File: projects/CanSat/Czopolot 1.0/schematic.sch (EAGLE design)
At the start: 16 parts

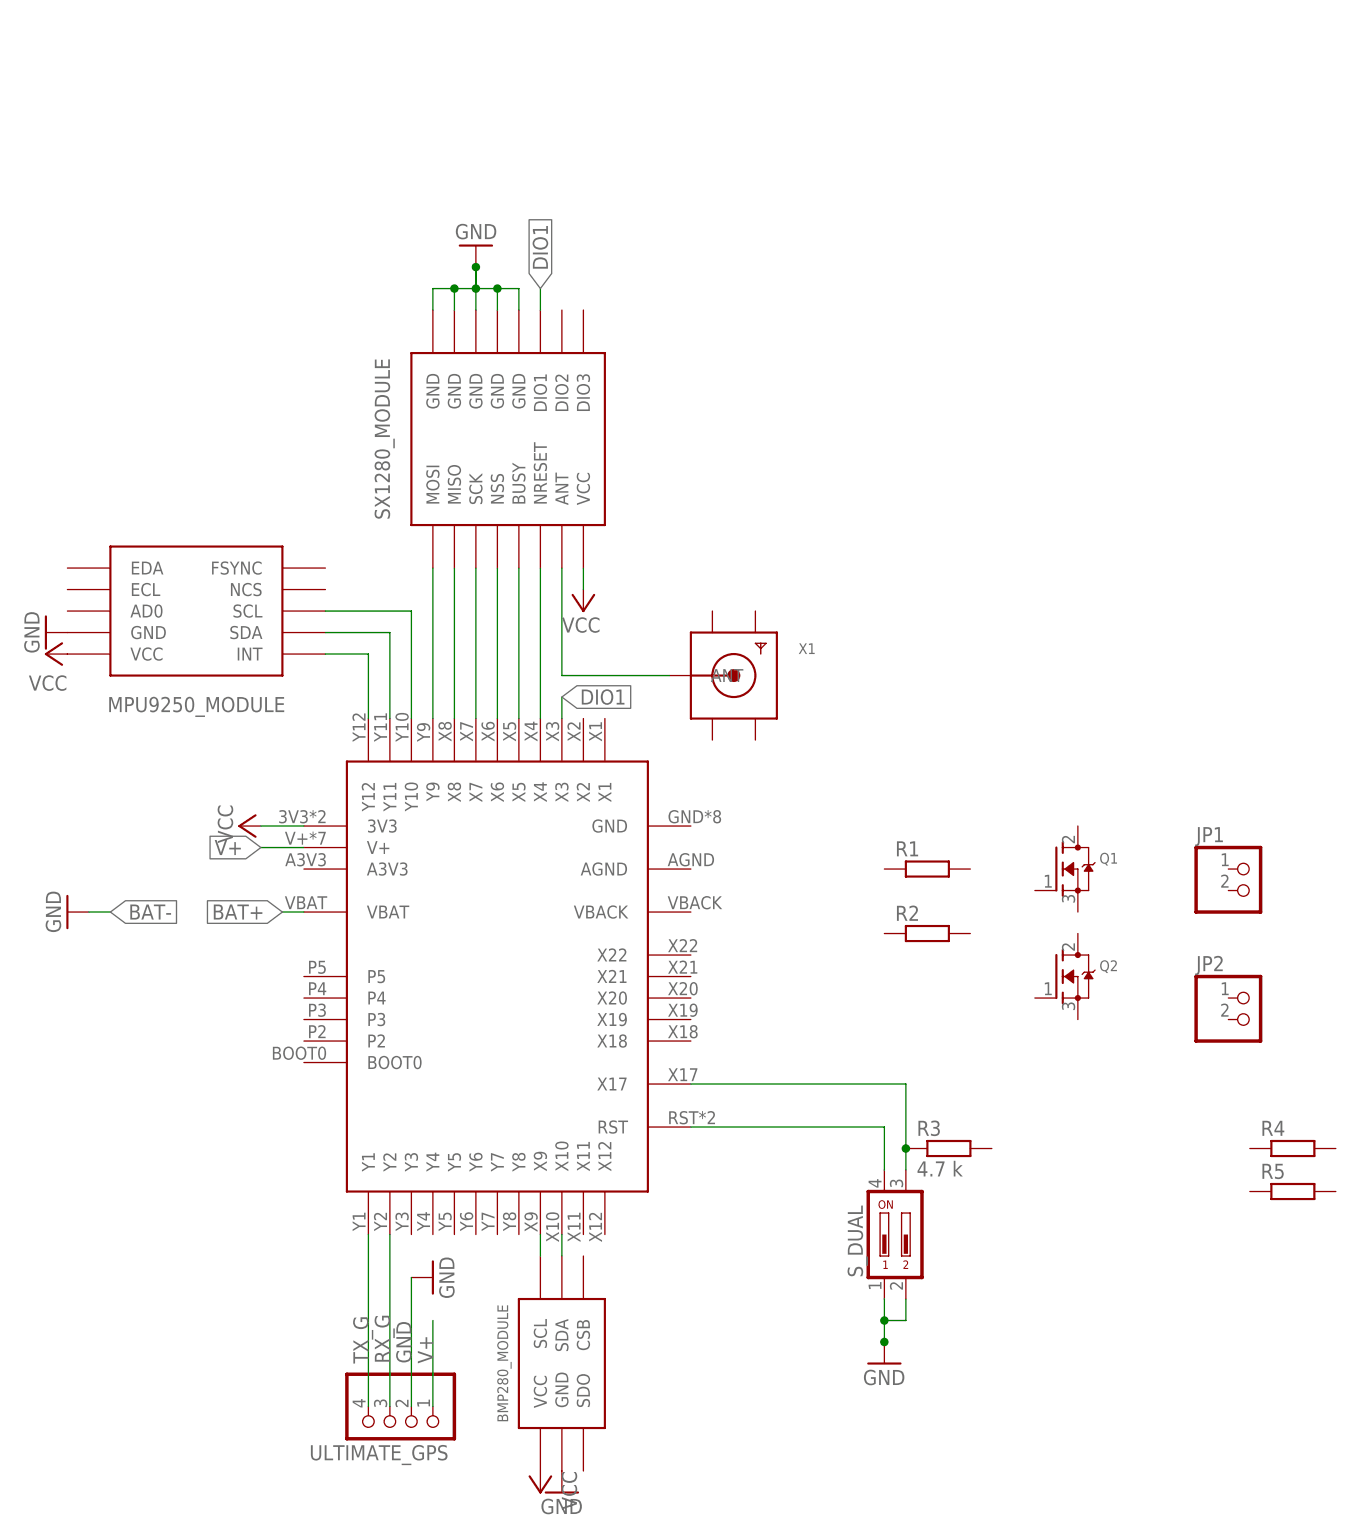
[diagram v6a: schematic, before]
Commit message: Switched SX1280
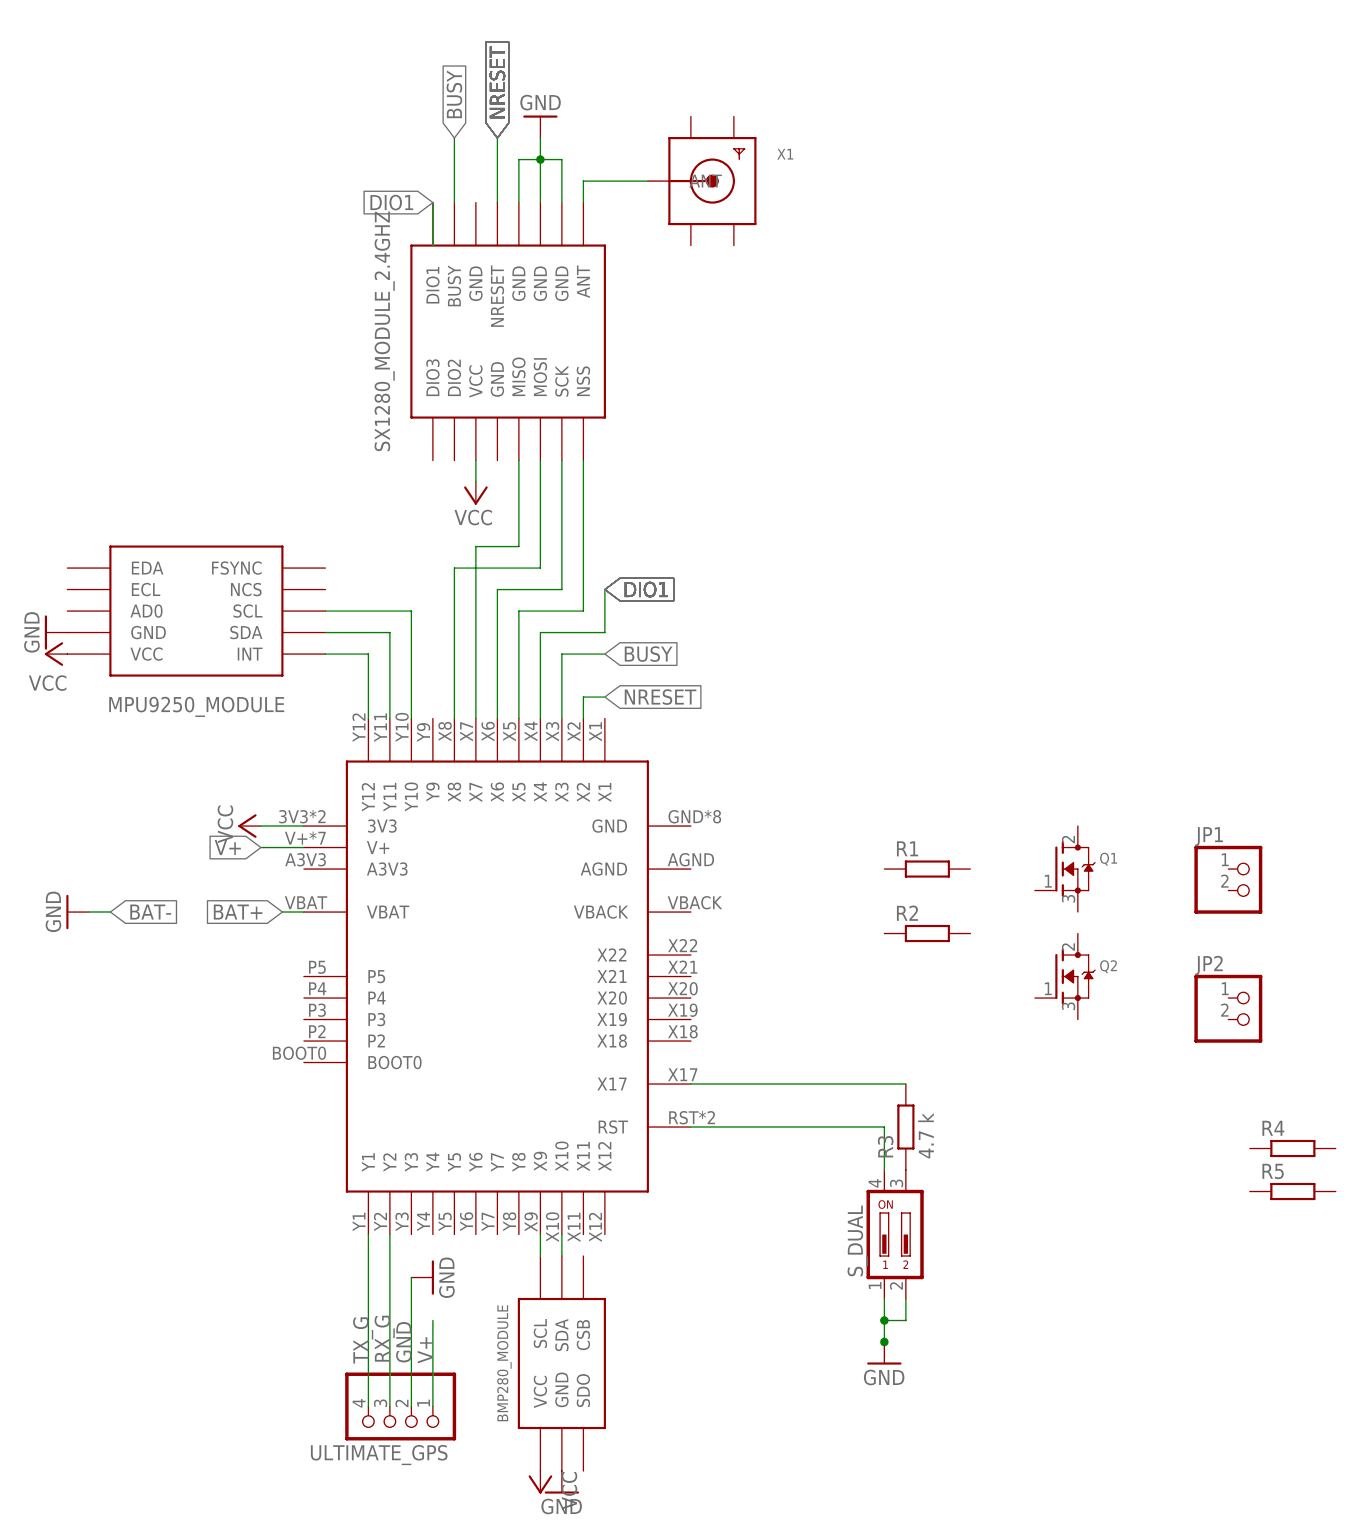
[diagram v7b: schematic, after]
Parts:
- removed U$2: SX1280, SobieskiSat2:SX1280
- added U$6: SX1280_2.4GHZ, SobieskiSat2:SX1280_2.4GHZ
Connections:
- new net BUSY: U$1.X3, U$6.BUSY
- new net NRESET: U$1.X2, U$6.NRESET
- net DIO1: now also U$1.X4; no longer U$1.X3, U$2.DIO1
- net GND: now also U$6.GND@3, U$6.GND@4, U$6.GND@5; no longer U$2.GND@1, U$2.GND@2, U$2.GND@3, U$2.GND@4, U$2.GND@5
- net N$1: now also U$1.X5, U$6.NSS; no longer U$1.Y9, U$2.MOSI
- net N$14: now also R3.2; no longer R3.1, U$5.3
- net N$2: now also U$1.X6, U$6.SCK; no longer U$1.X8, U$2.MISO
- net N$3: now also U$1.X8, U$6.MOSI; no longer U$1.X7, U$2.SCK
- net N$4: now also U$1.X7, U$6.MISO; no longer U$1.X6, U$2.NSS
- net N$5: now also U$6.ANT, X1.ANT; no longer U$1.X5, U$2.BUSY
- net N$6: now also U$6.DIO1; no longer U$1.X4, U$2.NRESET
- net N$7: now also R3.1, U$5.3; no longer U$2.ANT, X1.ANT
- net VCC: now also U$6.VCC; no longer U$2.VCC
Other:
- moved on the sheet: R3, X1
